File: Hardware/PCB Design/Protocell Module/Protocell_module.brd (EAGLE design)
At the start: 70.8 x 27.9 mm, 19 parts, among them IC1 MC7805BDTRKG, X3 RJ45-8X

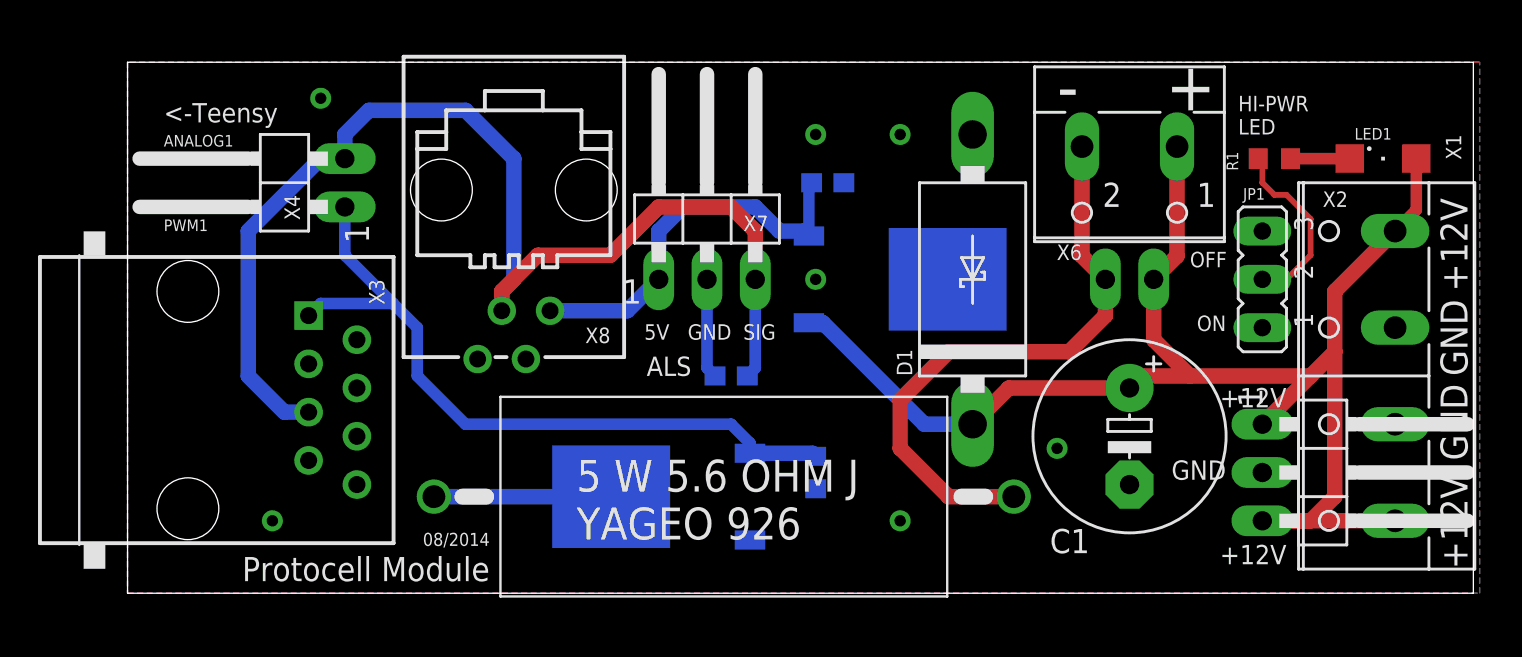
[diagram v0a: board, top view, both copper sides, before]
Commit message: changed terminal direction shrunk board size
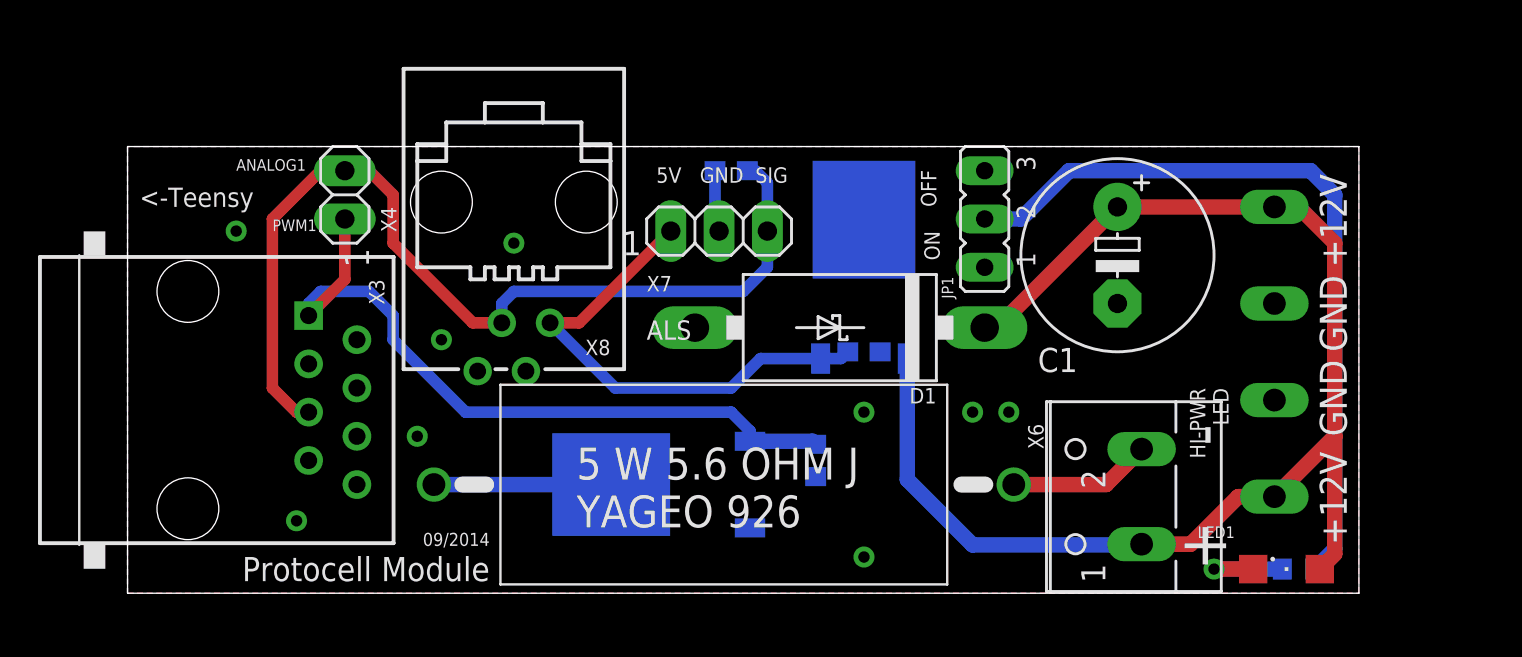
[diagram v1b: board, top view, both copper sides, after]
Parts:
- removed X2: (no value), CBLA_Test_bed_Library:1X03/90
- removed X5: (no value), CBLA_Test_bed_Library:1X02/90
- X4: device CBLA_Test_bed_Library:1X02/90 -> CBLA_Test_bed_Library:1X02
- X7: device CBLA_Test_bed_Library:1X03/90 -> CBLA_Test_bed_Library:1X03
- moved LED1 22.2 mm to (61.0, 1.27)
- moved R1 21.6 mm to (61.6, 1.27), flipped to the bottom
- moved X6 17.2 mm to (52.1, 5.08), turned to 90 degrees
- moved JP1 14.9 mm to (45.1, 19.7)
- moved C3 10.8 mm to (31.8, 22.2)
- moved C1 9.55 mm to (52.1, 17.8)
- moved C2 9.09 mm to (38.7, 12.7)
- moved D1 7.43 mm to (37.5, 14.0), turned to 180 degrees
- moved X1 6.48 mm to (59.7, 12.7), flipped to the bottom, turned to 270 degrees
- moved X4 3.86 mm to (11.4, 21.0)
- moved IC1 2.01 mm to (38.7, 17.1), turned to 0 degrees
- moved X7 1.42 mm to (31.1, 19.1)
- moved X8 0.64 mm to (20.3, 19.7)
- moved R2 0.64 mm to (36.2, 6.99)
- moved R3 0.63 mm to (31.1, 5.71)
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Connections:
- net +12V: no longer X2.1, X2.3, X5.1
- net GND: no longer X2.2
- net N$3: no longer X5.2
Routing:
- net PWR_LED_GND: track 9.66 -> 40.1 mm
- net N$3: track 31.6 -> 7.50 mm
- net ANALOG1: track 62.8 -> 50.8 mm
- net +12V: track 79.3 -> 72.0 mm
- net +5V: track 20.9 -> 26.2 mm
- net N$10: track 3.12 -> 5.66 mm, vias 0 -> 1
- net GND: track 5.25 -> 3.26 mm, vias 7 -> 9
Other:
- board size 70.8 x 27.9 mm -> 64.8 x 23.5 mm
- board text added: "09/2014"
- board text removed: "08/2014"

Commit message: Updated the board design
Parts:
- moved JP1 18.5 mm to (50.2, 1.91), turned to 0 degrees
- moved X6 13.7 mm to (48.9, 18.4), turned to 180 degrees
- moved C1 8.47 mm to (50.2, 9.53), turned to 90 degrees
- moved C2 2.54 mm to (38.7, 10.2)
- moved D1 0.90 mm to (36.8, 13.3)
- moved R3 0.90 mm to (30.5, 5.08)
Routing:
- net +12V: track 72.0 -> 47.3 mm
- net PWR_LED_GND: track 40.1 -> 15.9 mm
- net N$3: track 7.50 -> 25.2 mm
- net N$1: track 9.33 -> 10.6 mm
- net +5V: track 26.2 -> 27.4 mm
- added copper zone on layer 1, net +12V
- added copper zone on layer 16, net +12V
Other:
- board size 64.8 x 23.5 mm -> 64.8 x 24.1 mm
- board text added: "10/2014"
- board text added: "by PBAI & UWaterloo"
- board text removed: "09/2014"
